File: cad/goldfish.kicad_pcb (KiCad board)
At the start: 2 copper layers, 17.8 x 33 mm, 23 parts, among them J1 USB-C, J2 01x02, J3 01x12, J4 01x12, J5 01x05, U1 ATmega32U4, X1 16MHz

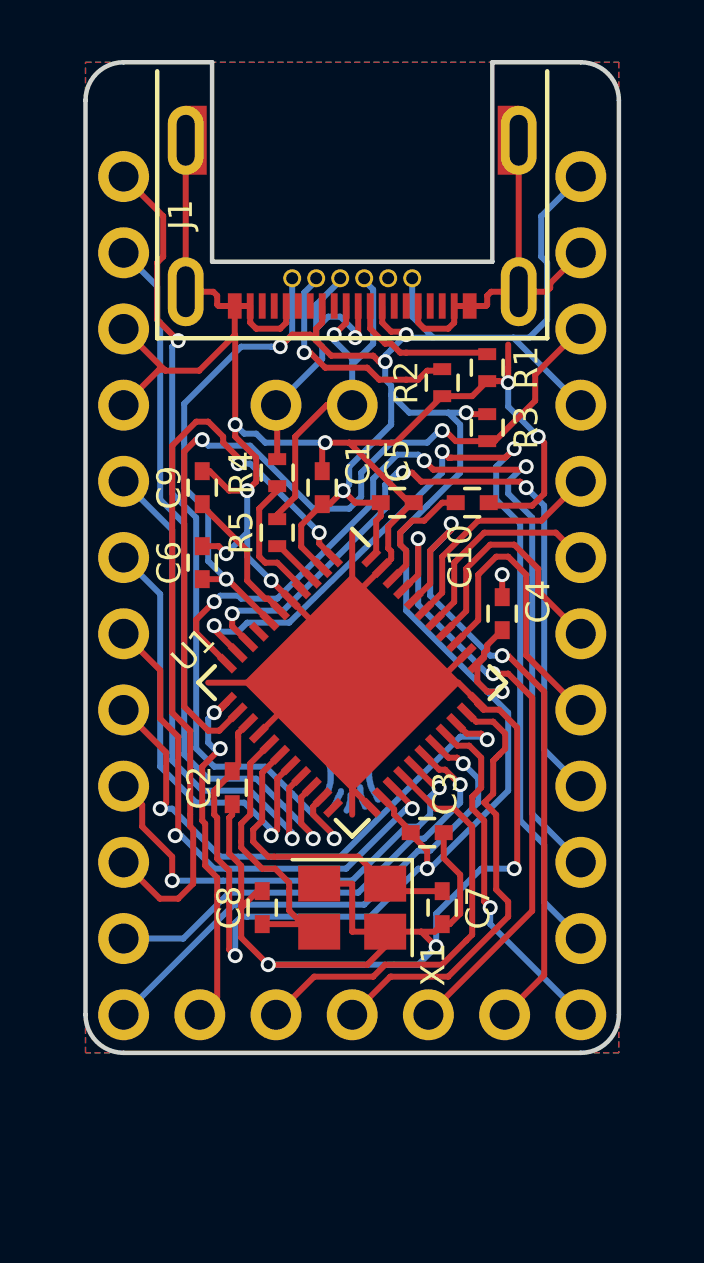
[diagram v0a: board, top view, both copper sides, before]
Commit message: Rev. A - Changed footprint of C6 from 0402 to 0603 to reduce component cost
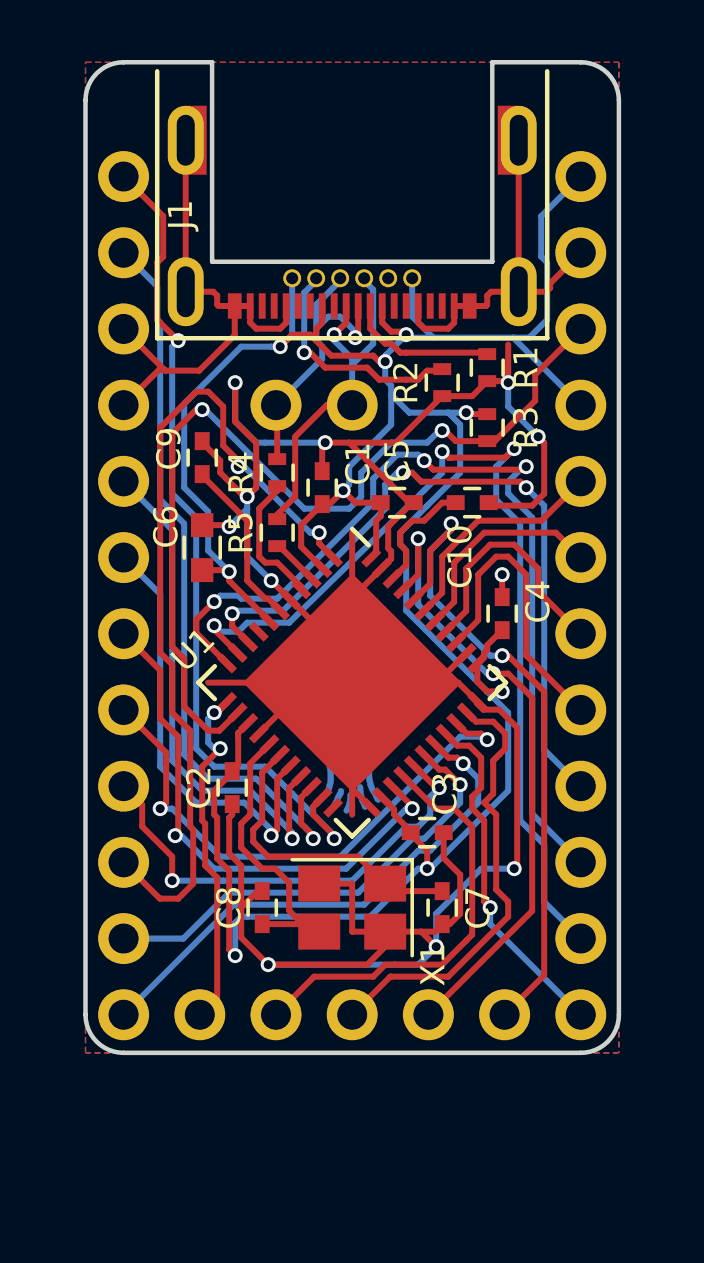
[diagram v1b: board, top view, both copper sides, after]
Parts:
- C6: footprint Capacitors_SMD:C_0402 -> Capacitors_SMD:C_0603
- moved C9 1.00 mm to (25.0, 32.5)
- moved C6 0.50 mm to (25.0, 35.5)
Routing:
- net /PE6: track 25.9 -> 28.3 mm
- net /RESET: track 29.0 -> 30.7 mm
- net Net-(C9-Pad1): track 4.68 -> 5.68 mm
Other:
- board text added: "Released under the Creative Commons Attribution Share-Alike 4.0 License https://creativecommons.org/licenses/by-sa/4.0/ Original Arduino Mini Design by Team Arduino Arduino Pro Mini Design by Spark Fun Electronics Pro Micro Design by Spark Fun Electronics Goldfish Design by Dr Derivative Changes in Rev. A: Changed footprint of C6 from 0402 to 0603 to reduce component cost"
- board text added: "Rev.A"
- board text removed: "Released under the Creative Commons Attribution Share-Alike 4.0 License https://creativecommons.org/licenses/by-sa/4.0/ Original Arduino Mini Design by Team Arduino Arduino Pro Mini Design by Spark Fun Electronics Pro Micro Design by Spark Fun Electronics Goldfish Design by Dr Derivative"
- board text removed: "rev.0"

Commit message: Rev. B - Fixed split keyboard issue and tidied up layout
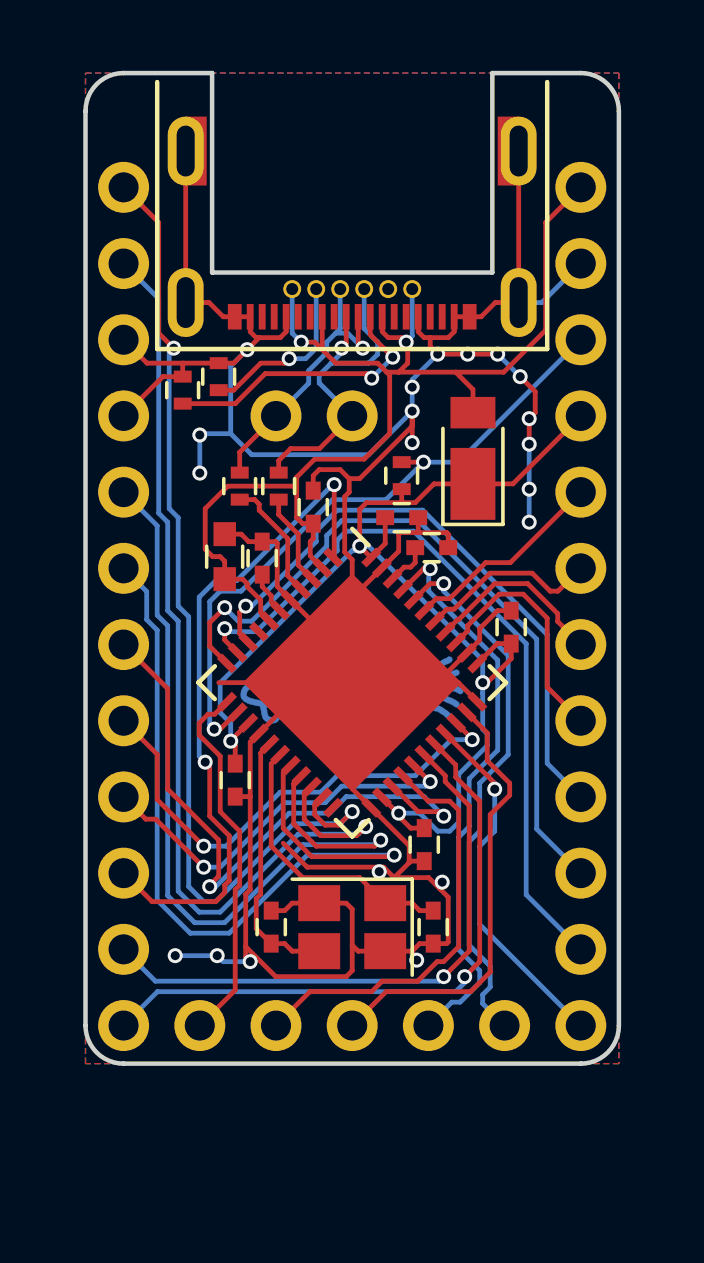
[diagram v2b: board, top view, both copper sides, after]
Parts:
- added D1: D_Schottky, Diodes_SMD:D_PowerDI-123, F.Cu at (34.0, 32.5)
- moved R1 10.2 mm to (24.4, 30.2), turned to 270 degrees
- moved C1 10.2 mm to (26.1, 43.2), turned to 270 degrees
- moved R2 7.45 mm to (25.6, 29.8), turned to 270 degrees
- moved C3 7.40 mm to (35.3, 38.1), turned to 90 degrees
- moved C2 6.68 mm to (32.4, 45.4)
- moved C4 4.63 mm to (31.6, 34.5), turned to 0 degrees
- moved C9 3.90 mm to (27.0, 35.9)
- moved R3 3.27 mm to (31.6, 33.1), turned to 270 degrees
- moved C5 2.80 mm to (28.7, 34.1), turned to 90 degrees
- moved C10 2.02 mm to (32.6, 35.5)
- moved R5 1.55 mm to (27.6, 33.5)
- moved R4 1.33 mm to (26.2, 33.5)
- moved C6 0.81 mm to (25.8, 35.8)
- moved C8 0.72 mm to (27.3, 48.1)
- moved C7 0.72 mm to (32.7, 48.1)
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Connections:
- C5 pad 1: VCC -> VBUS
- C6 pad 1: VCC -> VBUS
- J1 pad A4: VCC -> VBUS
- J1 pad A9: VCC -> VBUS
- J1 pad B4: VCC -> VBUS
- J1 pad B9: VCC -> VBUS
- J3 pad 1: VCC -> VBUS
- U1 pad 2: VCC -> VBUS
- U1 pad 7: VCC -> VBUS
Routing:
- net VCC: track 97.3 -> 41.7 mm, vias 9 -> 4
- net VBUS: track 0.00 -> 41.4 mm, vias 0 -> 2
- net /PD0: track 14.9 -> 27.3 mm
- net /PD1: track 17.5 -> 27.7 mm
- net /RESET: track 30.7 -> 22.0 mm
- net /PD2: track 25.1 -> 33.0 mm
- net /PB2: track 32.1 -> 25.2 mm, vias 3 -> 1
- net /PB3: track 30.5 -> 24.5 mm, vias 3 -> 1
- net /PE6: track 28.3 -> 22.7 mm
- net /PD3: track 28.1 -> 33.5 mm
- net Net-(J1-PadA5): track 5.01 -> 9.42 mm, vias 0 -> 2
- net Net-(C9-Pad1): track 5.68 -> 1.44 mm
- net /PB4: track 15.3 -> 19.5 mm
- net /PF1: track 22.2 -> 18.1 mm, vias 2 -> 1
- net /PB1: track 24.3 -> 20.6 mm, vias 3 -> 1
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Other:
- net class Default: clearance 0.17 -> 0.16; trace_width 0.2 -> 0.16
- rule trace_clearance: 0.17 -> 0.16
- board text added: "RAW"
- board text added: "Rev.B"
- board text removed: "QC"
- board text removed: "Rev.A"

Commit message: Rev. C - Changed bottom pins for Elite-C compatibility
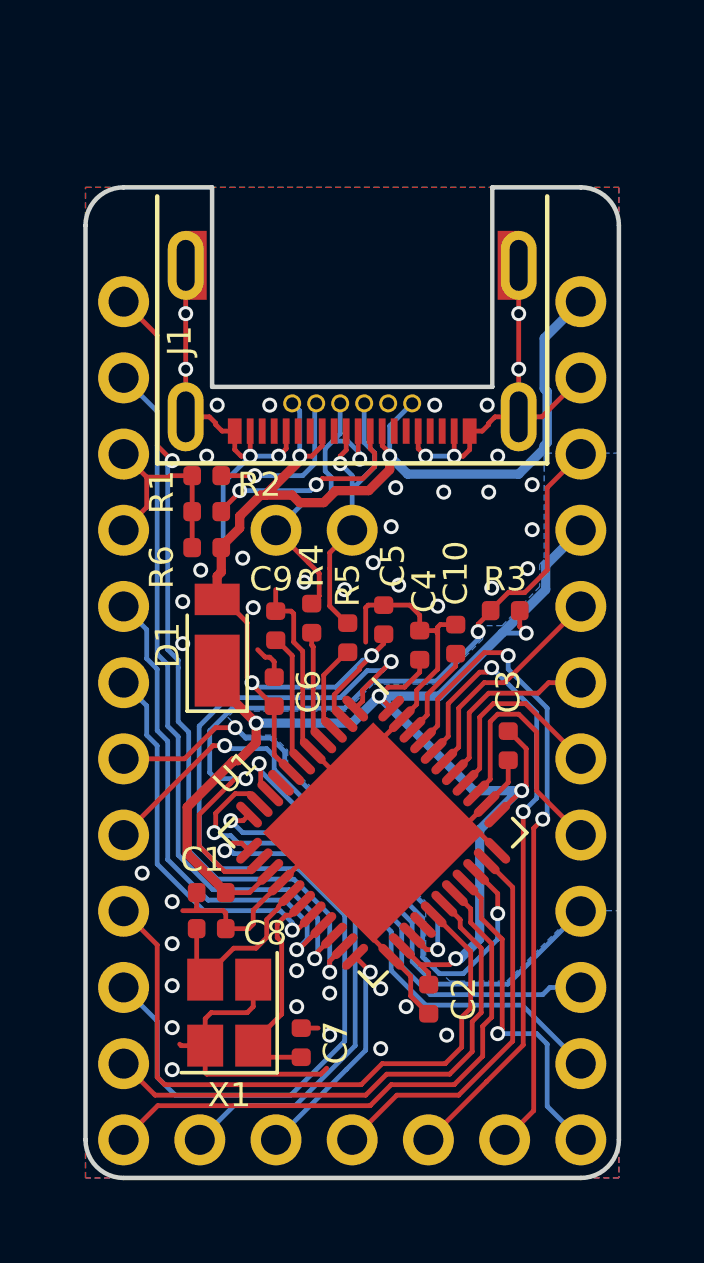
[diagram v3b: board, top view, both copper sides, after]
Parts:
- removed the G*** at (30.0, 40.4)
- added G***: LOGO, fish:fish-cu, B.Cu at (30.0, 43.8)
- added R6: 10k, Resistor_SMD:R_0402_1005Metric, F.Cu at (25.1, 35.5)
- C1, C10, C2, C3, C4, C5, C7, C8, C9: footprint Capacitors_SMD:C_0402 -> Capacitor_SMD:C_0402_1005Metric
- C6: footprint Capacitors_SMD:C_0603 -> Capacitor_SMD:C_0402_1005Metric
- D1: footprint Diodes_SMD:D_PowerDI-123 -> Diode_SMD:D_PowerDI-123
- J1: footprint USB Type-C:CX70M-24P1 -> usb-type-c:CX70M-24P1
- J2: footprint Pins:Pins2 -> pins:Pins2
- J3, J4: footprint Pins:Pins12 -> pins:Pins12
- J5: footprint Pins:Pins5 -> pins:Pins5
- R1, R2, R3, R4, R5: footprint Resistors_SMD:R_0402 -> Resistor_SMD:R_0402_1005Metric
- U1: footprint Housings_DFN_QFN:QFN-44-1EP_7x7mm_Pitch0.5mm -> Package_DFN_QFN:QFN-44-1EP_7x7mm_P0.5mm_EP5.2x5.2mm
- X1: footprint Crystals:Crystal_SMD_SeikoEpson_FA238-4pin_3.2x2.5mm -> Crystal:Crystal_SMD_SeikoEpson_FA238-4Pin_3.2x2.5mm
- moved D1 10.6 mm to (25.5, 38.8)
- moved C7 5.85 mm to (28.3, 52.0), turned to 90 degrees
- moved R3 5.67 mm to (35.1, 37.6), turned to 0 degrees
- moved R5 5.55 mm to (29.9, 38.5)
- moved C2 5.15 mm to (32.5, 50.5)
- moved U1 5.05 mm to (30.7, 45.0)
- moved R4 5.01 mm to (28.6, 37.9)
- moved X1 4.99 mm to (25.9, 51.0), turned to 90 degrees
- moved C6 4.79 mm to (27.4, 40.3)
- moved C5 4.43 mm to (31.1, 37.9)
- moved C4 4.29 mm to (32.2, 38.8), turned to 90 degrees
- moved R1 4.13 mm to (25.1, 34.3), turned to 0 degrees
- moved C3 3.95 mm to (35.2, 42.1), turned to 270 degrees
- moved C1 3.83 mm to (25.3, 47.0), turned to 180 degrees
- moved J2 3.81 mm to (27.5, 34.9)
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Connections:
- J1 pad A10: (no net) -> Net-(J1-PadA10)
- J1 pad A11: (no net) -> Net-(J1-PadA11)
- J1 pad A2: (no net) -> Net-(J1-PadA2)
- J1 pad A3: (no net) -> Net-(J1-PadA3)
- J1 pad A8: (no net) -> Net-(J1-PadA8)
- J1 pad B10: (no net) -> Net-(J1-PadB10)
- J1 pad B11: (no net) -> Net-(J1-PadB11)
- J1 pad B2: (no net) -> Net-(J1-PadB2)
- J1 pad B3: (no net) -> Net-(J1-PadB3)
- J1 pad B8: (no net) -> Net-(J1-PadB8)
- J5 pad 1: /PF1 -> /PF0
- J5 pad 2: /PF0 -> /PF1
- J5 pad 4: /PD6 -> /PD5
- U1 pad 22: (no net) -> /PD5
- U1 pad 26: /PD6 -> Net-(U1-Pad26)
- U1 pad 8: (no net) -> Net-(U1-Pad8)
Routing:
- net GND: track 153.6 -> 94.6 mm, vias 20 -> 46
- net /PD0: track 27.3 -> 13.0 mm
- net /PD6: track 14.1 -> 0.00 mm
- net /PE6: track 22.7 -> 34.1 mm, vias 2 -> 1
- net /PD1: track 27.7 -> 16.8 mm
- net /PB3: track 24.5 -> 15.6 mm
- net /PD7: track 13.1 -> 21.8 mm, vias 2 -> 0
- net /PD2: track 33.0 -> 24.6 mm
- net /PD5: track 0.00 -> 8.11 mm, vias 0 -> 1
- net VCC: track 41.7 -> 49.8 mm, vias 4 -> 5
- net /PB2: track 25.2 -> 18.7 mm
- net /PD3: track 33.5 -> 27.9 mm
- net /PD4: track 20.9 -> 15.9 mm
- net /PB7: track 12.4 -> 17.5 mm, vias 0 -> 1
- net /PC6: track 16.5 -> 20.9 mm
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- added copper zone on B.Cu, net VCC
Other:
- net class PWR added: clearance 0.16, trace_width 0.31, via_dia 0.5, via_drill 0.3
- board text added: "Rev.C"
- board text removed: "Rev.B"

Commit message: Update design files to KiCad 6.0
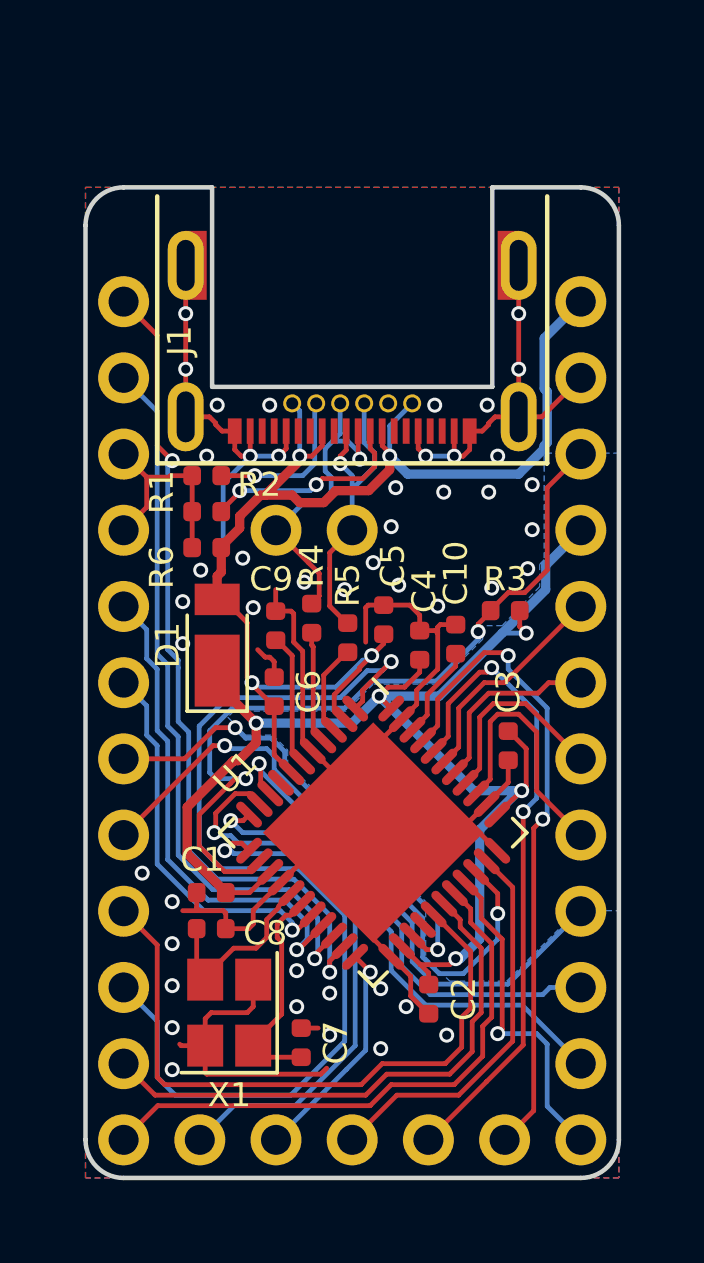
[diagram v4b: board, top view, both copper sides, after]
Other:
- net class Default removed
- net class PWR removed

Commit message: Fix silkscreen on bottom edge pins
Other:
- rule pad_to_mask_clearance: 0.2 -> 0
- board text added: "D5"
- board text added: "Released under the Creative Commons Attribution Share-Alike 4.0 License https://creativecommons.org/licenses/by-sa/4.0/ Original Arduino Mini Design by Team Arduino Arduino Pro Mini Design by Spark Fun Electronics Pro Micro Design by Spark Fun Electronics Goldfish Design by Lucas Jansen"
- board text added: "Rev.D"
- board text removed: "D6"
- board text removed: "Released under the Creative Commons Attribution Share-Alike 4.0 License https://creativecommons.org/licenses/by-sa/4.0/ Original Arduino Mini Design by Team Arduino Arduino Pro Mini Design by Spark Fun Electronics Pro Micro Design by Spark Fun Electronics Goldfish Design by Dr Derivative Changes in Rev. A: Changed footprint of C6 from 0402 to 0603 to reduce component cost"
- board text removed: "Rev.C"
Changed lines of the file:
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@@
     (title "Goldfish")
     (date "2017-12-20")
-    (rev "C")
+    (rev "D")
   )
   (layers
@@
   )
   (setup
-    (pad_to_mask_clearance 0.2)
+    (stackup
+      (layer "F.SilkS" (type "Top Silk Screen"))
+      (layer "F.Paste" (type "Top Solder Paste"))
+      (layer "F.Mask" (type "Top Solder Mask") (thickness 0.01))
+      (layer "F.Cu" (type "copper") (thickness 0.035))
+      (layer "dielectric 1" (type "core") (thickness 1.51) (material "FR4") (epsilon_r 4.5) (loss_tangent 0.02))
+      (layer "B.Cu" (type "copper") (thickness 0.035))
+      (layer "B.Mask" (type "Bottom Solder Mask") (thickness 0.01))
+      (layer "B.Paste" (type "Bottom Solder Paste"))
+      (layer "B.SilkS" (type "Bottom Silk Screen"))
+      (copper_finish "None")
+      (dielectric_constraints no)
+    )
+    (pad_to_mask_clearance 0)
     (grid_origin 30 40)
     (pcbplotparams
@@
   (gr_line (start 36.604 32.4816) (end 34.572 32.4816) (layer "B.SilkS") (width 0.15))
   (gr_line (start 23.4468 31.3132) (end 22.888 31.3132) (layer "B.SilkS") (width 0.15))
-  (gr_line (start 26.3932 35.5868) (end 26.3932 35.028) (layer "B.SilkS") (width 0.15))
-  (gr_line (start 22.888 35.5868) (end 23.4468 35.5868) (layer "B.SilkS") (width 0.15))
-  (gr_line (start 31.0668 35.5868) (end 31.0668 35.028) (layer "B.SilkS") (width 0.15))
-  (gr_line (start 26.3932 35.5868) (end 31.0668 35.5868) (layer "B.SilkS") (width 0.15))
+  (gr_line (start 26.3932 35.9868) (end 26.3932 35.428) (layer "B.SilkS") (width 0.15))
+  (gr_line (start 22.888 35.9868) (end 23.4468 35.9868) (layer "B.SilkS") (width 0.15))
+  (gr_line (start 31.0668 35.9868) (end 31.0668 35.428) (layer "B.SilkS") (width 0.15))
+  (gr_line (start 26.3932 35.9868) (end 31.0668 35.9868) (layer "B.SilkS") (width 0.15))
   (gr_line (start 23.4468 35.9868) (end 23.4468 31.3132) (layer "B.SilkS") (width 0.15))
   (gr_arc (start 21.11 24.76) (mid 21.481974 23.861974) (end 22.38 23.49) (layer "Edge.Cuts") (width 0.15))
@@
   (gr_line (start 21.11 24.76) (end 21.11 55.24) (layer "Edge.Cuts") (width 0.15))
   (gr_line (start 22.38 56.51) (end 37.62 56.51) (layer "Edge.Cuts") (width 0.15))
-  (gr_text "F0" (at 32.54 53.8176) (layer "B.SilkS")
+  (gr_text "F1" (at 32.54 53.8176) (layer "B.SilkS")
     (effects (font (size 0.8 0.8) (thickness 0.15)) (justify mirror))
   )
@@
     (effects (font (size 0.8 0.8) (thickness 0.15)) (justify mirror))
   )
-  (gr_text "USB" (at 28.73 36.3488) (layer "B.SilkS")
+  (gr_text "USB" (at 28.73 36.7488) (layer "B.SilkS")
     (effects (font (size 0.8 0.8) (thickness 0.15)) (justify mirror))
   )
@@
     (effects (font (size 0.8 0.8) (thickness 0.15)) (justify mirror))
   )
-  (gr_text "Rev.C" (at 30 51.938) (layer "B.SilkS")
+  (gr_text "Rev.D" (at 30 51.938) (layer "B.SilkS")
     (effects (font (size 0.8 0.8) (thickness 0.15)) (justify mirror))
   )
@@
     (effects (font (size 0.8 0.8) (thickness 0.15)) (justify left mirror))
   )
-  (gr_text "F1" (at 34.572 53.8176) (layer "B.SilkS")
+  (gr_text "F0" (at 34.572 53.8176) (layer "B.SilkS")
     (effects (font (size 0.8 0.8) (thickness 0.15)) (justify mirror))
   )
-  (gr_text "D6" (at 27.46 53.8176) (layer "B.SilkS")
+  (gr_text "D5" (at 27.46 53.8176) (layer "B.SilkS")
     (effects (font (size 0.8 0.8) (thickness 0.15)) (justify mirror))
   )
@@
     (effects (font (size 0.8 0.8) (thickness 0.15)) (justify mirror))
   )
-  (gr_text "Released under the Creative Commons Attribution Share-Alike 4.0 License\nhttps://creativecommons.org/licenses/by-sa/4.0/\n\nOriginal Arduino Mini Design by Team Arduino\nArduino Pro Mini Design by Spark Fun Electronics\nPro Micro Design by Spark Fun Electronics\nGoldfish Design by Dr Derivative\n\nChanges in Rev. A:\nChanged footprint of C6 from 0402 to 0603 to reduce component cost " (at 15 183) (layer "Dwgs.User")
+  (gr_text "Released under the Creative Commons Attribution Share-Alike 4.0 License\nhttps://creativecommons.org/licenses/by-sa/4.0/\n\nOriginal Arduino Mini Design by Team Arduino\nArduino Pro Mini Design by Spark Fun Electronics\nPro Micro Design by Spark Fun Electronics\nGoldfish Design by Lucas Jansen" (at 15 186) (layer "Dwgs.User")
     (effects (font (size 1.5 1.5) (thickness 0.2)) (justify left))
   )
